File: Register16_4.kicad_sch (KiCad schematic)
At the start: 4 parts

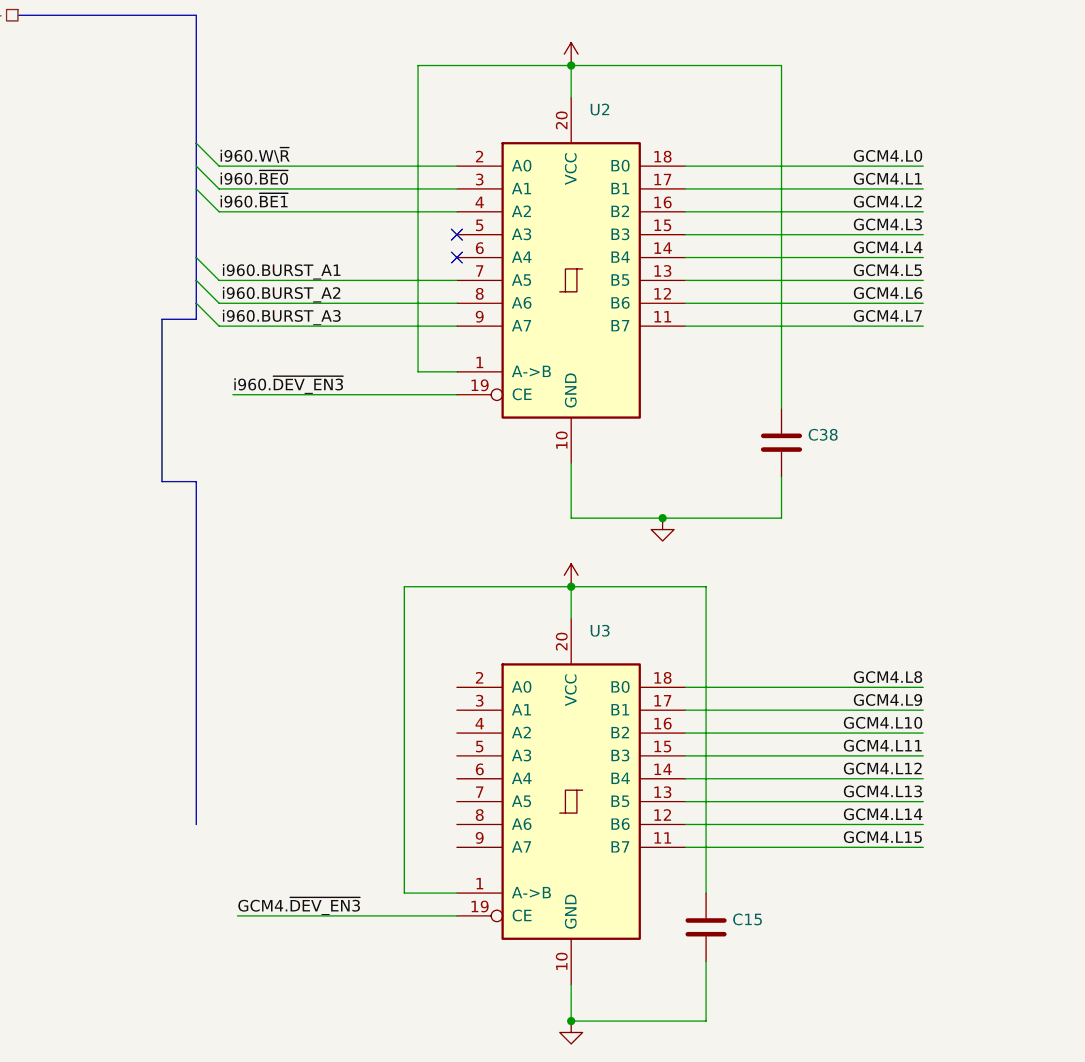
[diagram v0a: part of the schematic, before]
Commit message: Use an AHC157 for the deactivation of the interrupt lines while changes are being made to the CCLs
Instead of using tons of pullups and downs, use the AHC157 channel
feature. Channel 0 is the connection between CCLS and i960. Channel 1 is
a fixed pattern that is useful for booting and deactivating all
interrupts
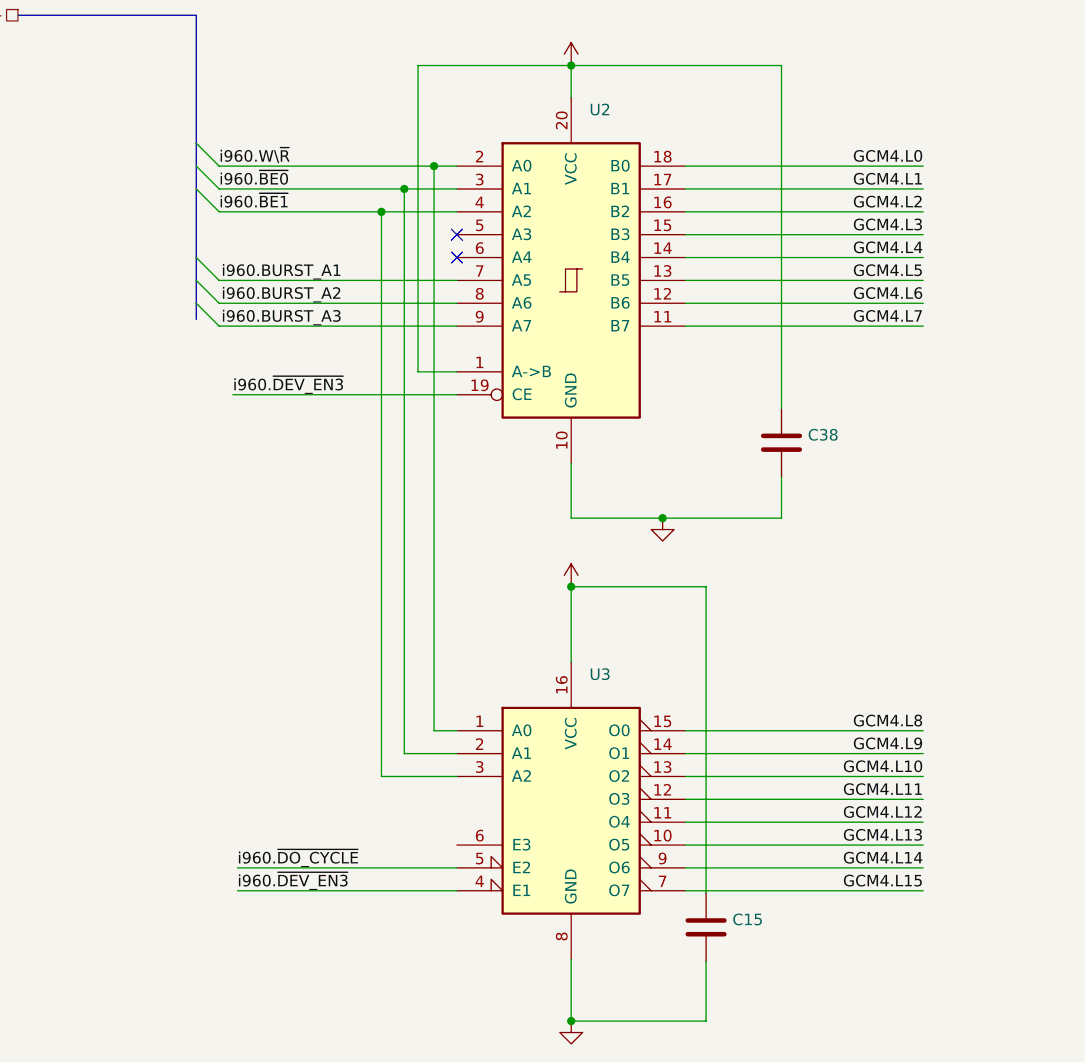
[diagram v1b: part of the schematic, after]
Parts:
- removed U3: (no value), symbol 74xx:74HC245
- added U3: (no value), symbol 74xx:74LS138
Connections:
- net GCM4.L10: now also U3.13 (O2)
- net GCM4.L11: now also U3.12 (O3)
- net GCM4.L12: now also U3.11 (O4)
- net GCM4.L13: now also U3.10 (O5)
- net GCM4.L14: now also U3.9 (O6)
- net GCM4.L15: now also U3.7 (O7)
- net GCM4.L8: now also U3.15 (O0)
- net GCM4.L9: now also U3.14 (O1)
- net GND: now also U3.8 (GND)
- net VCC: now also U3.16 (VCC)
- net i960.W\~{R}: now also U3.1 (A0)
- net i960.~{BE0}: now also U3.2 (A1)
- net i960.~{BE1}: now also U3.3 (A2)
- net i960.~{DEV_EN3}: now also U3.4 (E1)
- new net i960.~{DO_CYCLE}: U3.5 (E2)

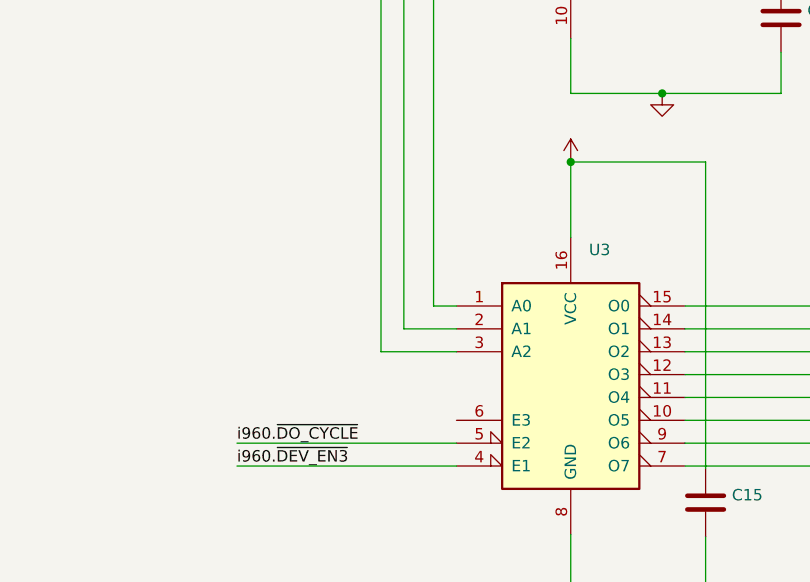
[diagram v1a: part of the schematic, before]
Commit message: Bound E3 to VCC on the AHC138
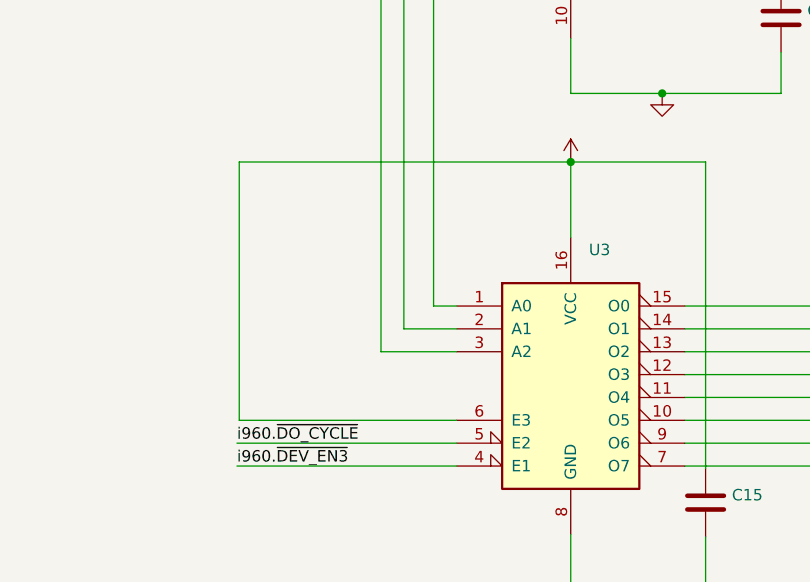
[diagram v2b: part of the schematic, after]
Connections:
- net VCC: now also U3.6 (E3)
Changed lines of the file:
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@@
+    (stroke (width 0) (type default) (color 0 0 0 0))
+  )
+  (wire (pts (xy 105.41 115.57) (xy 105.41 86.868))
     (stroke (width 0) (type default) (color 0 0 0 0))
   )
@@
     (stroke (width 0) (type default) (color 0 0 0 0))
   )
+  (wire (pts (xy 129.54 115.57) (xy 105.41 115.57))
+    (stroke (width 0) (type default) (color 0 0 0 0))
+  )
   (wire (pts (xy 121.158 45.212) (xy 129.54 45.212))
     (stroke (width 0) (type default) (color 0 0 0 0))
@@
     (stroke (width 0) (type default) (color 0 0 0 0))
   )
+  (wire (pts (xy 105.41 86.868) (xy 142.24 86.868))
+    (stroke (width 0) (type default) (color 0 0 0 0))
+  )

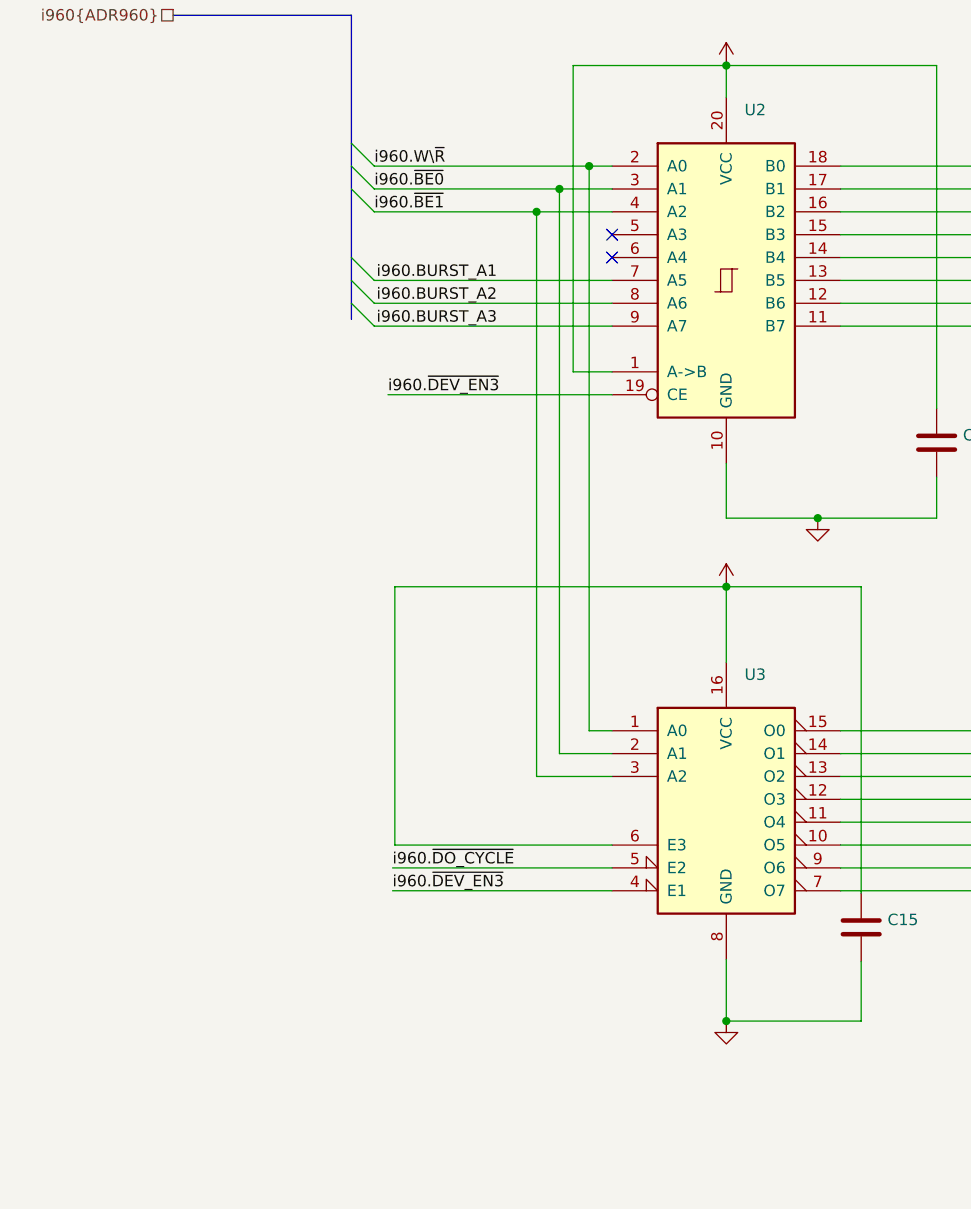
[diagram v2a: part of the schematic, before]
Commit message: Update the AHC138 to have the following pattern:
High bits to Low bits

Bit 2) W/~{R}
Bit 1) ~{BE0}
Bit 0) ~{BE1}

The byte enable bits are reversed to make the output easier brain out
since they are active low.
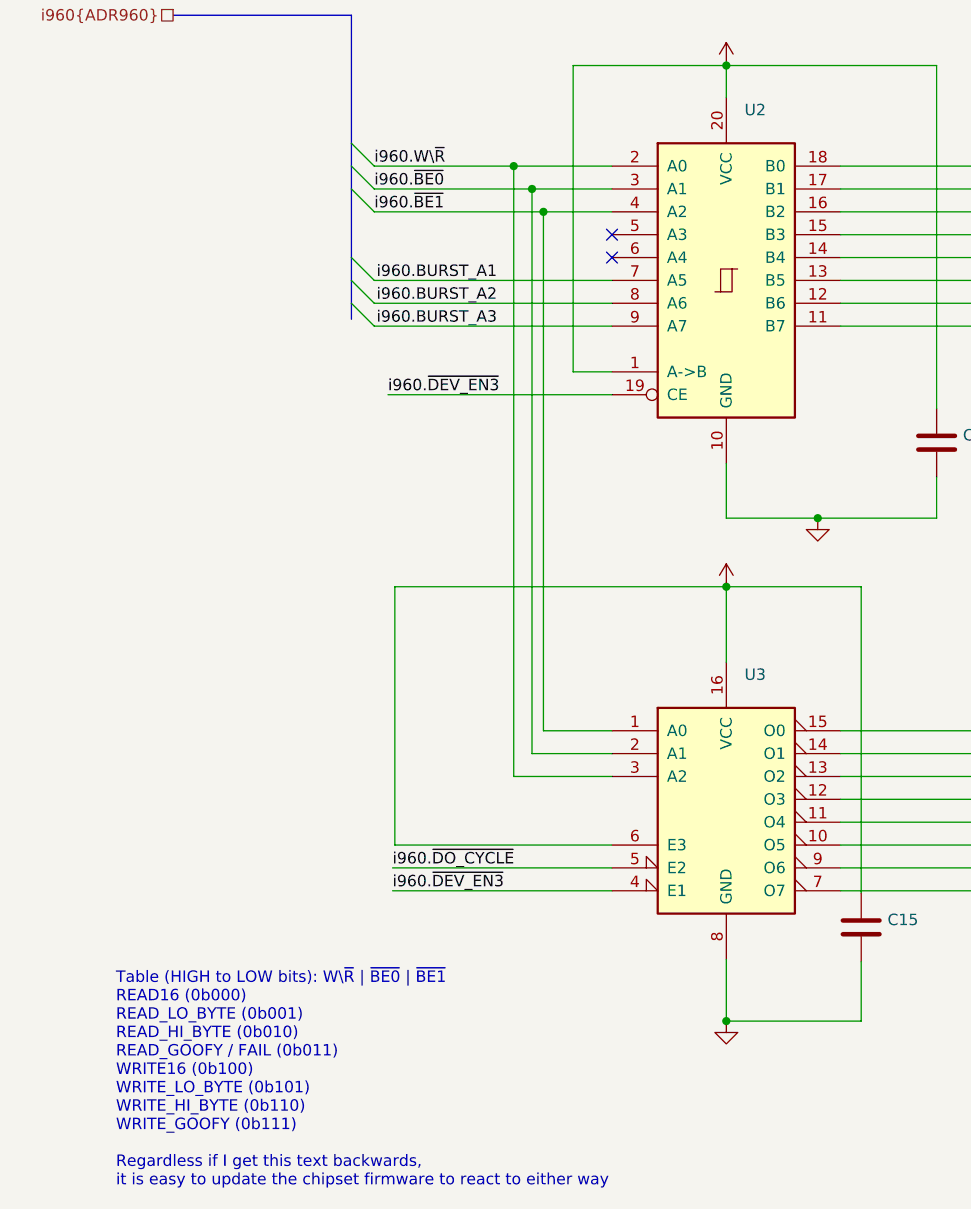
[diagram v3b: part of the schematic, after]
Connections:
- net i960.W\~{R}: now also U3.3 (A2); no longer U3.1 (A0)
- net i960.~{BE1}: now also U3.1 (A0); no longer U3.3 (A2)
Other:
- note added: "Table (HIGH to LOW bits): W\~{R} | ~{BE0} | ~{BE1} READ16 (0b000) READ_LO_BYTE (0b001) READ_HI_BYTE (0b010) READ_GOOFY / FAIL (0b011) WRITE16 (0b100) WRITE_LO_BYTE (0b101) WRITE_HI_BYTE (0b110) WRITE_GOOFY (0b111) Regardless if I get this text backwards, it is easy to update the chipset firmware to react to either way"
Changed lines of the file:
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@@
     (comment 1 "Extraneous information that should not use its own gpios")
   )
-  (junction (at 123.698 42.672) (diameter 0) (color 0 0 0 0)
-  )
-  (junction (at 121.158 45.212) (diameter 0) (color 0 0 0 0)
+  (junction (at 121.92 45.212) (diameter 0) (color 0 0 0 0)
   )
   (junction (at 142.24 86.868) (diameter 0) (color 0 0 0 0)
   )
-  (junction (at 127 40.132) (diameter 0) (color 0 0 0 0)
+  (junction (at 118.618 40.132) (diameter 0) (color 0 0 0 0)
   )
   (junction (at 152.4 79.248) (diameter 0) (color 0 0 0 0)
@@
   )
   (junction (at 142.24 28.956) (diameter 0) (color 0 0 0 0)
+  )
+  (junction (at 120.65 42.672) (diameter 0) (color 0 0 0 0)
   )
   (no_connect (at 129.54 47.752))
@@
     (stroke (width 0) (type default) (color 0 0 0 0))
   )
-  (wire (pts (xy 121.158 107.95) (xy 121.158 45.212))
-    (stroke (width 0) (type default) (color 0 0 0 0))
-  )
   (wire (pts (xy 105.41 115.57) (xy 105.41 86.868))
     (stroke (width 0) (type default) (color 0 0 0 0))
   )
-  (wire (pts (xy 103.124 45.212) (xy 121.158 45.212))
-    (stroke (width 0) (type default) (color 0 0 0 0))
-  )
   (wire (pts (xy 154.94 50.292) (xy 181.356 50.292))
     (stroke (width 0) (type default) (color 0 0 0 0))
@@
     (stroke (width 0) (type default) (color 0 0 0 0))
   )
-  (wire (pts (xy 103.124 40.132) (xy 127 40.132))
+  (wire (pts (xy 129.54 105.41) (xy 120.65 105.41))
     (stroke (width 0) (type default) (color 0 0 0 0))
   )
@@
     (stroke (width 0) (type default) (color 0 0 0 0))
   )
-  (wire (pts (xy 127 40.132) (xy 129.54 40.132))
+  (wire (pts (xy 118.618 40.132) (xy 129.54 40.132))
+    (stroke (width 0) (type default) (color 0 0 0 0))
+  )
+  (wire (pts (xy 103.124 40.132) (xy 118.618 40.132))
     (stroke (width 0) (type default) (color 0 0 0 0))
   )
@@
     (stroke (width 0) (type default) (color 0 0 0 0))
   )
-  (wire (pts (xy 123.698 42.672) (xy 129.54 42.672))
-    (stroke (width 0) (type default) (color 0 0 0 0))
-  )
   (bus (pts (xy 224.028 30.226) (xy 241.808 30.226))
     (stroke (width 0) (type default) (color 0 0 0 0))
   )
+  (wire (pts (xy 121.92 45.212) (xy 129.54 45.212))
+    (stroke (width 0) (type default) (color 0 0 0 0))
+  )
   (wire (pts (xy 165.608 67.056) (xy 165.608 28.956))
     (stroke (width 0) (type default) (color 0 0 0 0))
@@
     (stroke (width 0) (type default) (color 0 0 0 0))
   )
-  (wire (pts (xy 121.158 45.212) (xy 129.54 45.212))
-    (stroke (width 0) (type default) (color 0 0 0 0))
-  )
-  (wire (pts (xy 129.54 107.95) (xy 121.158 107.95))
-    (stroke (width 0) (type default) (color 0 0 0 0))
-  )
-  (wire (pts (xy 129.54 105.41) (xy 123.698 105.41))
+  (wire (pts (xy 121.92 102.87) (xy 121.92 45.212))
+    (stroke (width 0) (type default) (color 0 0 0 0))
+  )
+  (wire (pts (xy 103.124 45.212) (xy 121.92 45.212))
     (stroke (width 0) (type default) (color 0 0 0 0))
   )
@@
     (stroke (width 0) (type default) (color 0 0 0 0))
   )
+  (wire (pts (xy 129.54 102.87) (xy 121.92 102.87))
+    (stroke (width 0) (type default) (color 0 0 0 0))
+  )
   (wire (pts (xy 142.24 79.248) (xy 152.4 79.248))
     (stroke (width 0) (type default) (color 0 0 0 0))
@@
     (stroke (width 0) (type default) (color 0 0 0 0))
   )
-  (wire (pts (xy 103.124 42.672) (xy 123.698 42.672))
+  (wire (pts (xy 118.618 107.95) (xy 118.618 40.132))
+    (stroke (width 0) (type default) (color 0 0 0 0))
+  )
+  (wire (pts (xy 129.54 107.95) (xy 118.618 107.95))
+    (stroke (width 0) (type default) (color 0 0 0 0))
+  )
+  (wire (pts (xy 103.124 42.672) (xy 120.65 42.672))
     (stroke (width 0) (type default) (color 0 0 0 0))
   )
@@
     (stroke (width 0) (type default) (color 0 0 0 0))
   )
+  (wire (pts (xy 120.65 42.672) (xy 129.54 42.672))
+    (stroke (width 0) (type default) (color 0 0 0 0))
+  )
   (wire (pts (xy 105.41 86.868) (xy 142.24 86.868))
     (stroke (width 0) (type default) (color 0 0 0 0))
@@
     (stroke (width 0) (type default) (color 0 0 0 0))
   )
-  (wire (pts (xy 123.698 105.41) (xy 123.698 42.672))
-    (stroke (width 0) (type default) (color 0 0 0 0))
-  )
-  (wire (pts (xy 129.54 102.87) (xy 127 102.87))
-    (stroke (width 0) (type default) (color 0 0 0 0))
-  )
-  (wire (pts (xy 127 102.87) (xy 127 40.132))
+  (wire (pts (xy 120.65 42.672) (xy 120.65 105.41))
     (stroke (width 0) (type default) (color 0 0 0 0))
   )
@@
     (stroke (width 0) (type default) (color 0 0 0 0))
   )
+  (text "Table (HIGH to LOW bits): W\\~{R} | ~{BE0} | ~{BE1}\nREAD16 (0b000)\nREAD_LO_BYTE (0b001)\nREAD_HI_BYTE (0b010)\nREAD_GOOFY / FAIL (0b011)\nWRITE16 (0b100)\nWRITE_LO_BYTE (0b101)\nWRITE_HI_BYTE (0b110)\nWRITE_GOOFY (0b111)\n\nRegardless if I get this text backwards, \nit is easy to update the chipset firmware to react to either way"
+    (at 74.422 153.67 0)
+    (effects (font (size 1.27 1.27)) (justify left bottom))
+  )
   (label "GCM4.L8" (at 181.356 102.87 180)
